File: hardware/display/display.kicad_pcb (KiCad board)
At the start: 4 copper layers, 98 x 67 mm, 411 parts, among them J1 Power Connector, J2 Data Connector

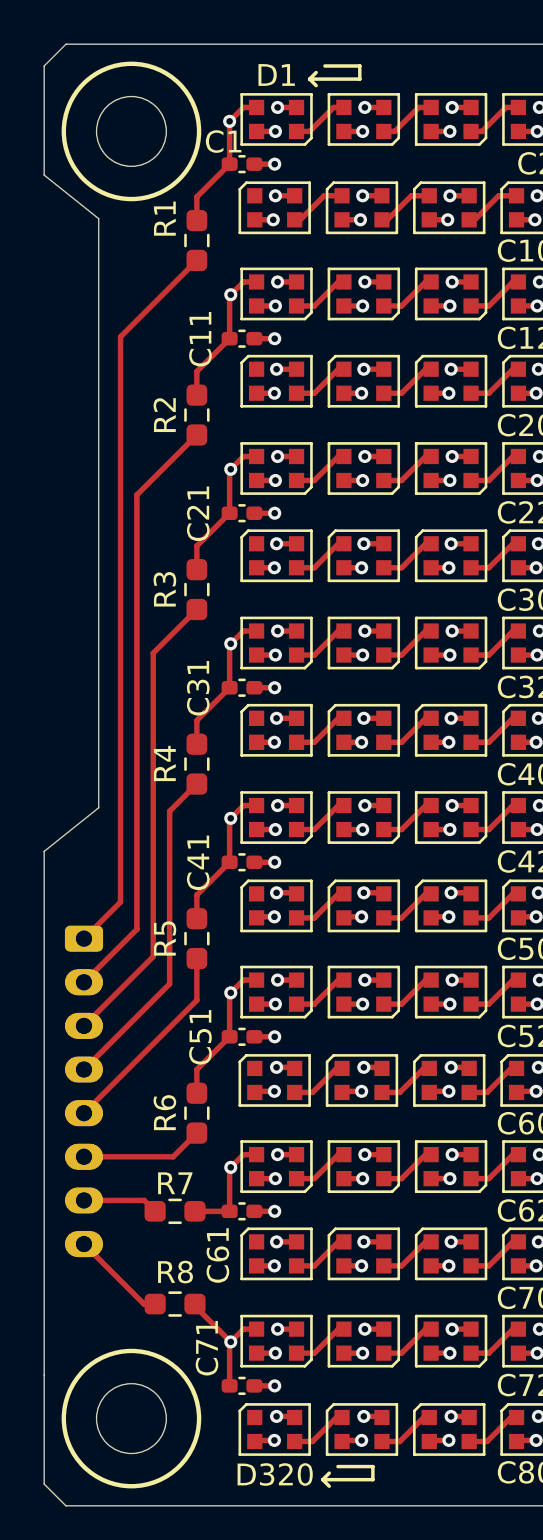
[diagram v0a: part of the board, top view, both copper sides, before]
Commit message: Data Line Cleanup
Moved some resistors and removed old, unnecessary vias.
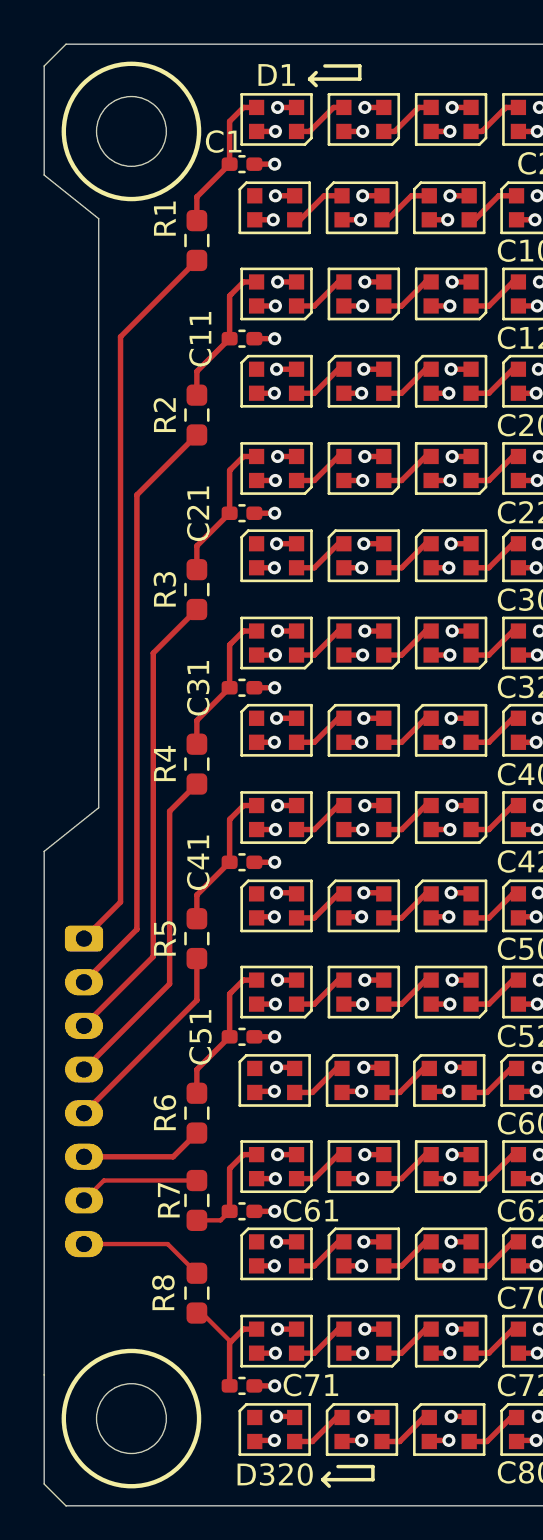
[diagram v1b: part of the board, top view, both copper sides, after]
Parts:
- moved R7 1.12 mm to (14.0, 65.0), turned to -90 degrees
- moved R8 1.12 mm to (14.0, 69.2), turned to -90 degrees
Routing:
- net DIN7: track 3.79 -> 5.88 mm
- net DIN8: track 4.40 -> 5.73 mm
- net Net-(D281-DIN): track 5.90 -> 5.56 mm, vias 1 -> 0
- net Net-(D1-DIN): track 6.73 -> 6.67 mm, vias 1 -> 0
- net Net-(D81-DIN): track 6.69 -> 6.67 mm, vias 1 -> 0
- net Net-(D41-DIN): track 6.69 -> 6.67 mm, vias 1 -> 0
- net Net-(D201-DIN): track 6.69 -> 6.67 mm, vias 1 -> 0
- net Net-(D161-DIN): track 6.69 -> 6.67 mm, vias 1 -> 0
- net Net-(D121-DIN): track 6.69 -> 6.67 mm, vias 1 -> 0
- net Net-(D241-DIN): track 5.15 -> 5.13 mm, vias 1 -> 0

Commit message: Will Meeting
Added JLC constraints
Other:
- rule pad_to_mask_clearance: 0 -> 0.038
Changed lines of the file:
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@@
 			(dielectric_constraints no)
 		)
-		(pad_to_mask_clearance 0)
+		(pad_to_mask_clearance 0.038)
+		(solder_mask_min_width 0.23)
 		(allow_soldermask_bridges_in_footprints no)
 		(tenting front back)
@@
 		(model "${KICAD9_3DMODEL_DIR}/LED_SMD.3dshapes/LED_WS2812B-2020_PLCC4_2.0x2.0mm.step"
 			(offset
-				(xyz 0 0 0)
+				(xyz 0 0.3 0)
 			)
 			(scale
@@
 			)
 			(rotate
-				(xyz 0 0 0)
+				(xyz -0 -0 -0)
 			)
 		)
@@
 			(pinfunction "Pin_1")
 			(pintype "passive")
-			(zone_connect 2)
+			(zone_connect 1)
 		)
 		(pad "2" thru_hole circle
@@
 			(pinfunction "Pin_2")
 			(pintype "passive")
-			(zone_connect 2)
+			(zone_connect 1)
 			(thermal_bridge_angle 0)
 		)
@@
 		)
 		(embedded_fonts no)
-		(model "C:/Users/Jacob/Engineering/Electronics/OPS 2/esp32-handheld/libraries/esp_32_handheld.3dshapes/EEV-FK1E102Q.stp"
+		(model "C:/Users/Jacob/Engineering/Electronics/esp32-handheld/libraries/esp_32_handheld.3dshapes/EEV-FK1E102Q.stp"
 			(offset
 				(xyz 0 0 0)
@@
 		(fill yes
 			(thermal_gap 0.5)
-			(thermal_bridge_width 0.5)
+			(thermal_bridge_width 1)
 		)
 		(polygon
@@
 		(fill yes
 			(thermal_gap 0.5)
-			(thermal_bridge_width 0.5)
+			(thermal_bridge_width 1)
 		)
 		(polygon

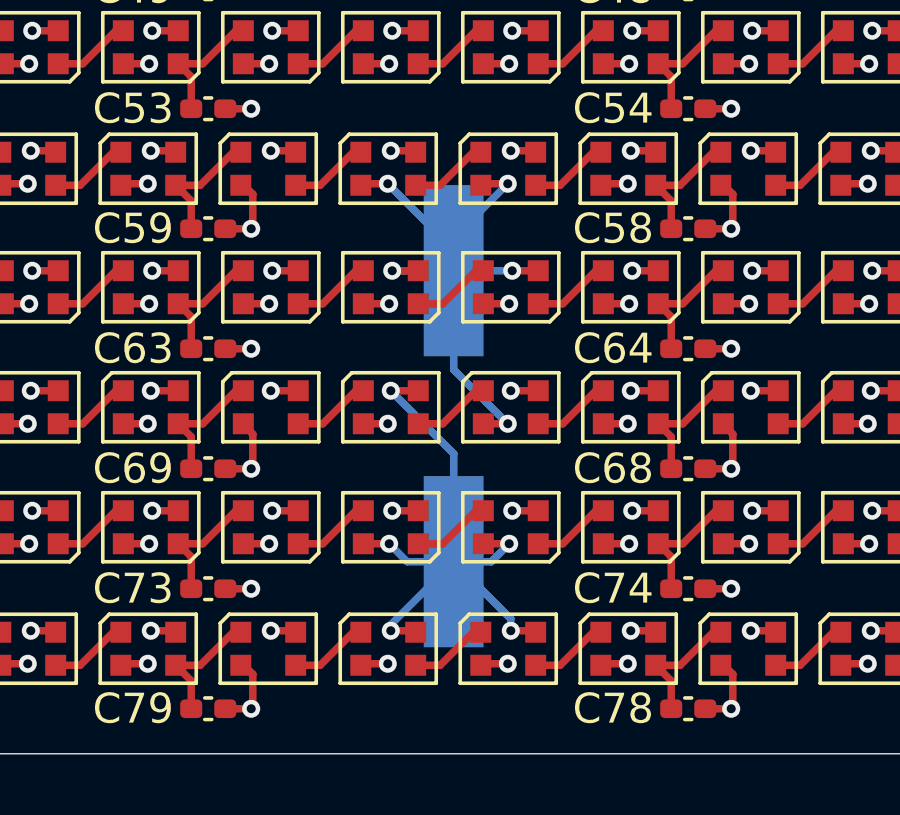
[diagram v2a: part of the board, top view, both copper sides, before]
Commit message: Added assembly part numbers and schematic caps
Linked LCSC part numbers for LEDs, decoupling caps, and data resistors.

Added 10, 100uF caps in schematic, but footprints are needed still.
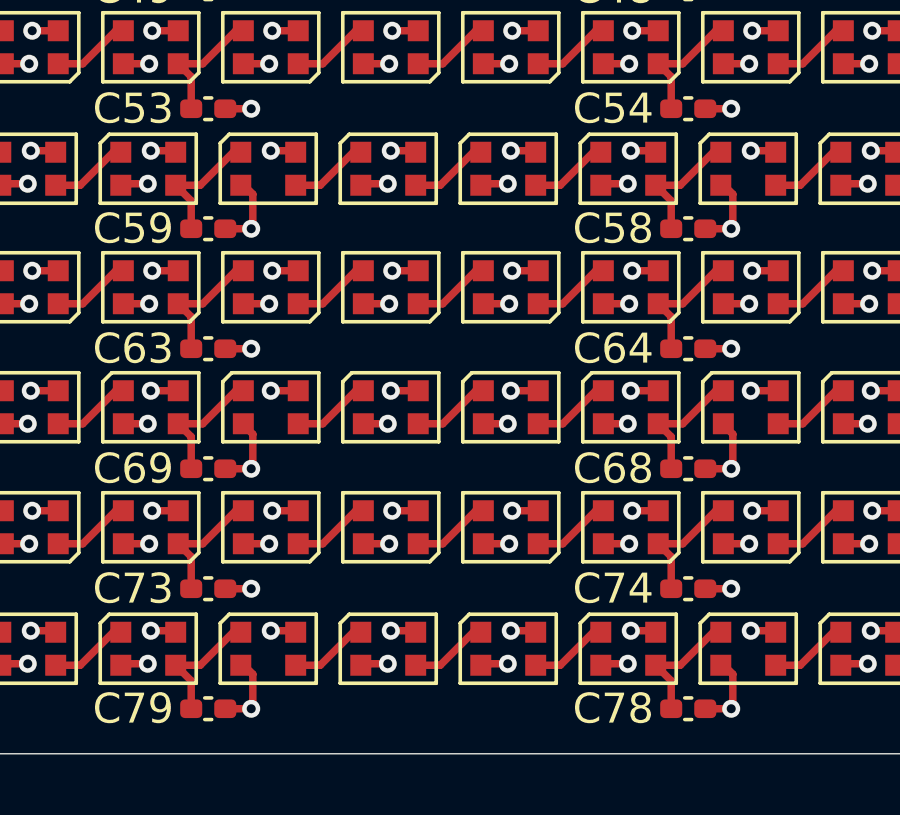
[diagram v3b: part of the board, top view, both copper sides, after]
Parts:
- removed C81: 1000uF, esp32_handheld:EEEFK0J332AQ
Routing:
- net VDD: track 297.3 -> 280.0 mm
- net GND: track 385.1 -> 367.8 mm
